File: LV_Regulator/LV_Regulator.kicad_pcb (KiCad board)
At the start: 4 copper layers, 150 x 100 mm, 199 parts, among them IC1 UCC12040DVE, IC2 MIC29152WU, IC3 MIC29152WU, J1 430450400, J2 430450400, J3 430450800, J4 430450800, J5 SWD, J6 2169890001, K1 41.52.9.005.0010, Q1 BC807, U1 ADM2483xRW, U2 STM32F103C8Tx, U3 25CSM04xxSN, U4 BQ25858QWRRVRQ1, U5 CSD19506KTT, U6 CSD19506KTT, U7 CSD19506KTT, U8 CSD19506KTT, Y1 32.768kHz, Y2 8MHz

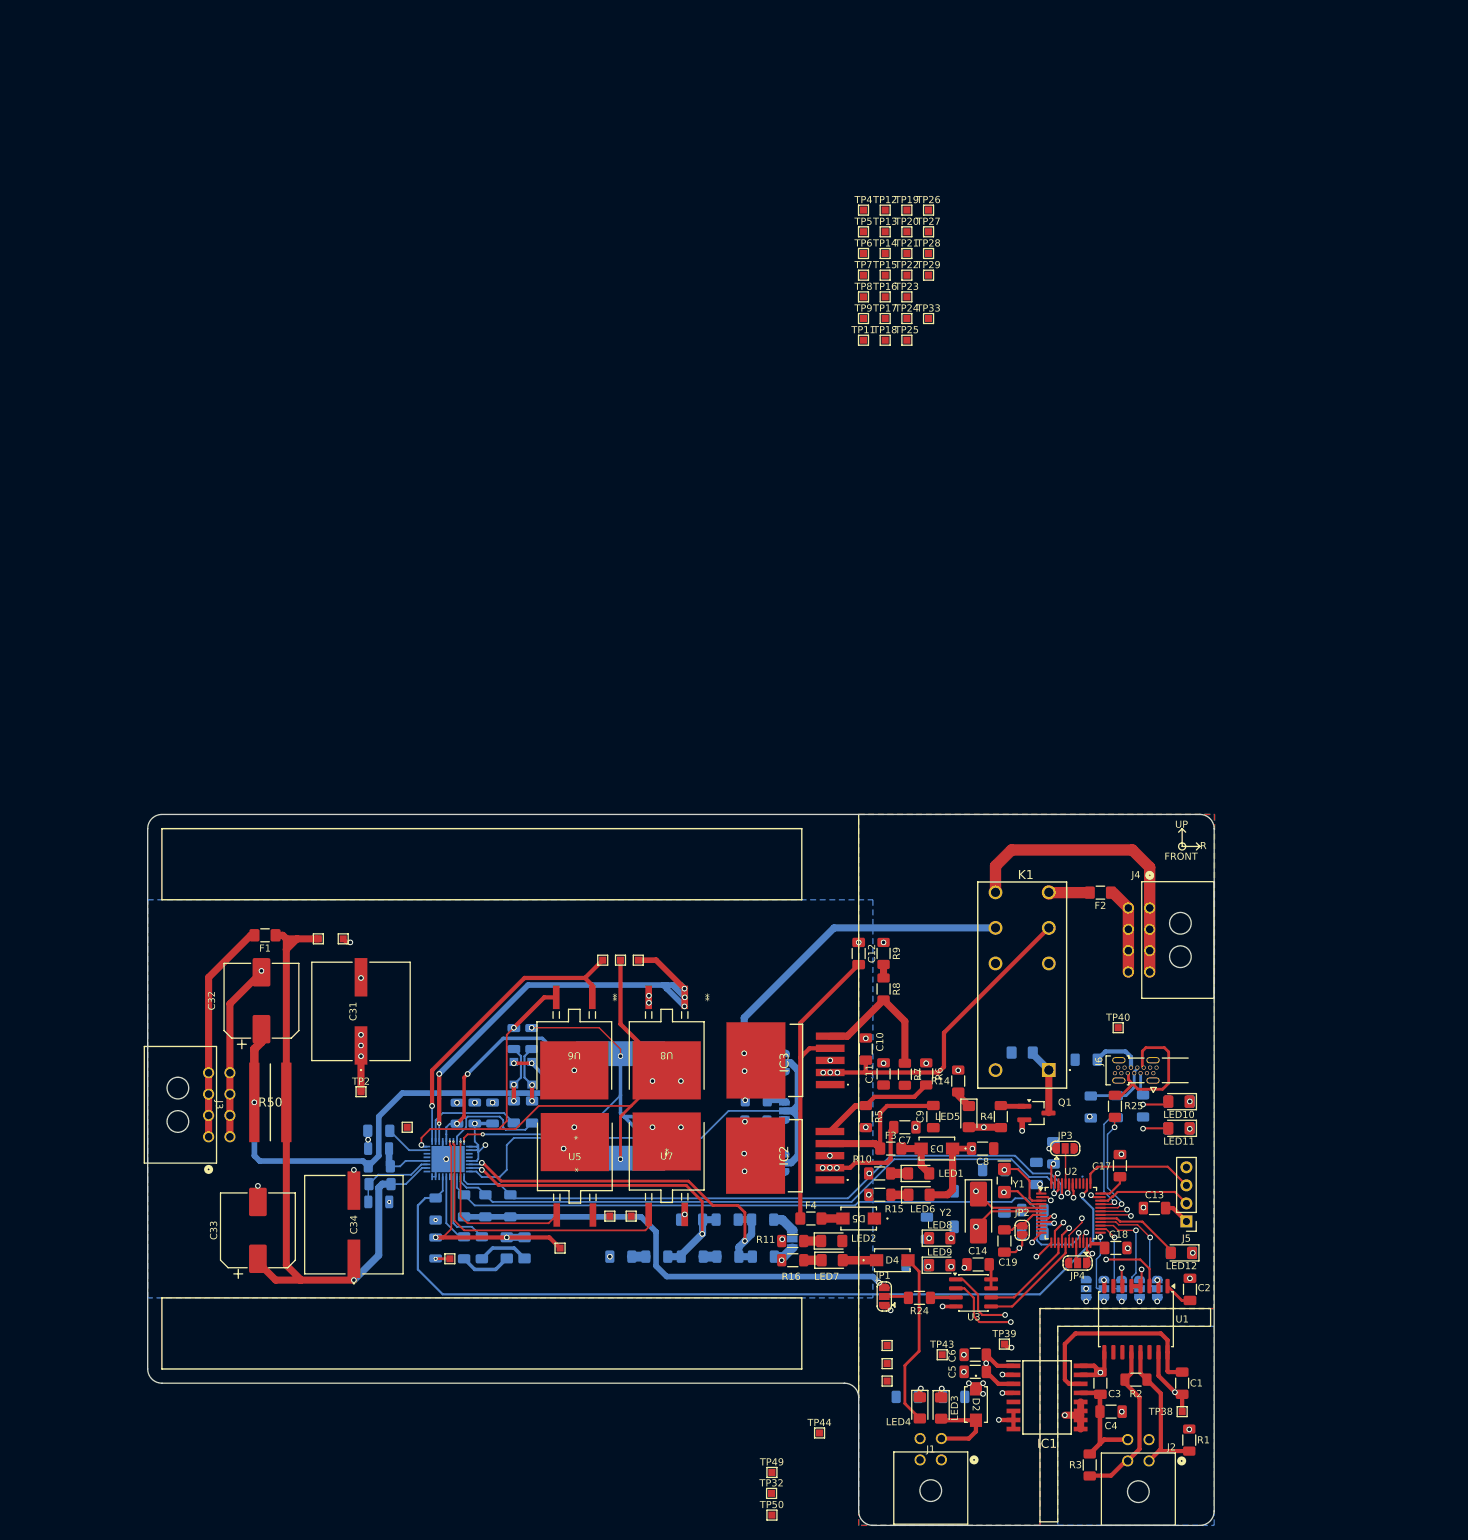
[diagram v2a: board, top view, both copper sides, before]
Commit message: Deleted Draft Regulator and Test Points Routing
Deleted Draft Routing of the Regulator and Power Electronics side of the board, because layout was not optimal in the slightest, & will replace and re-route the whole power electronics side.
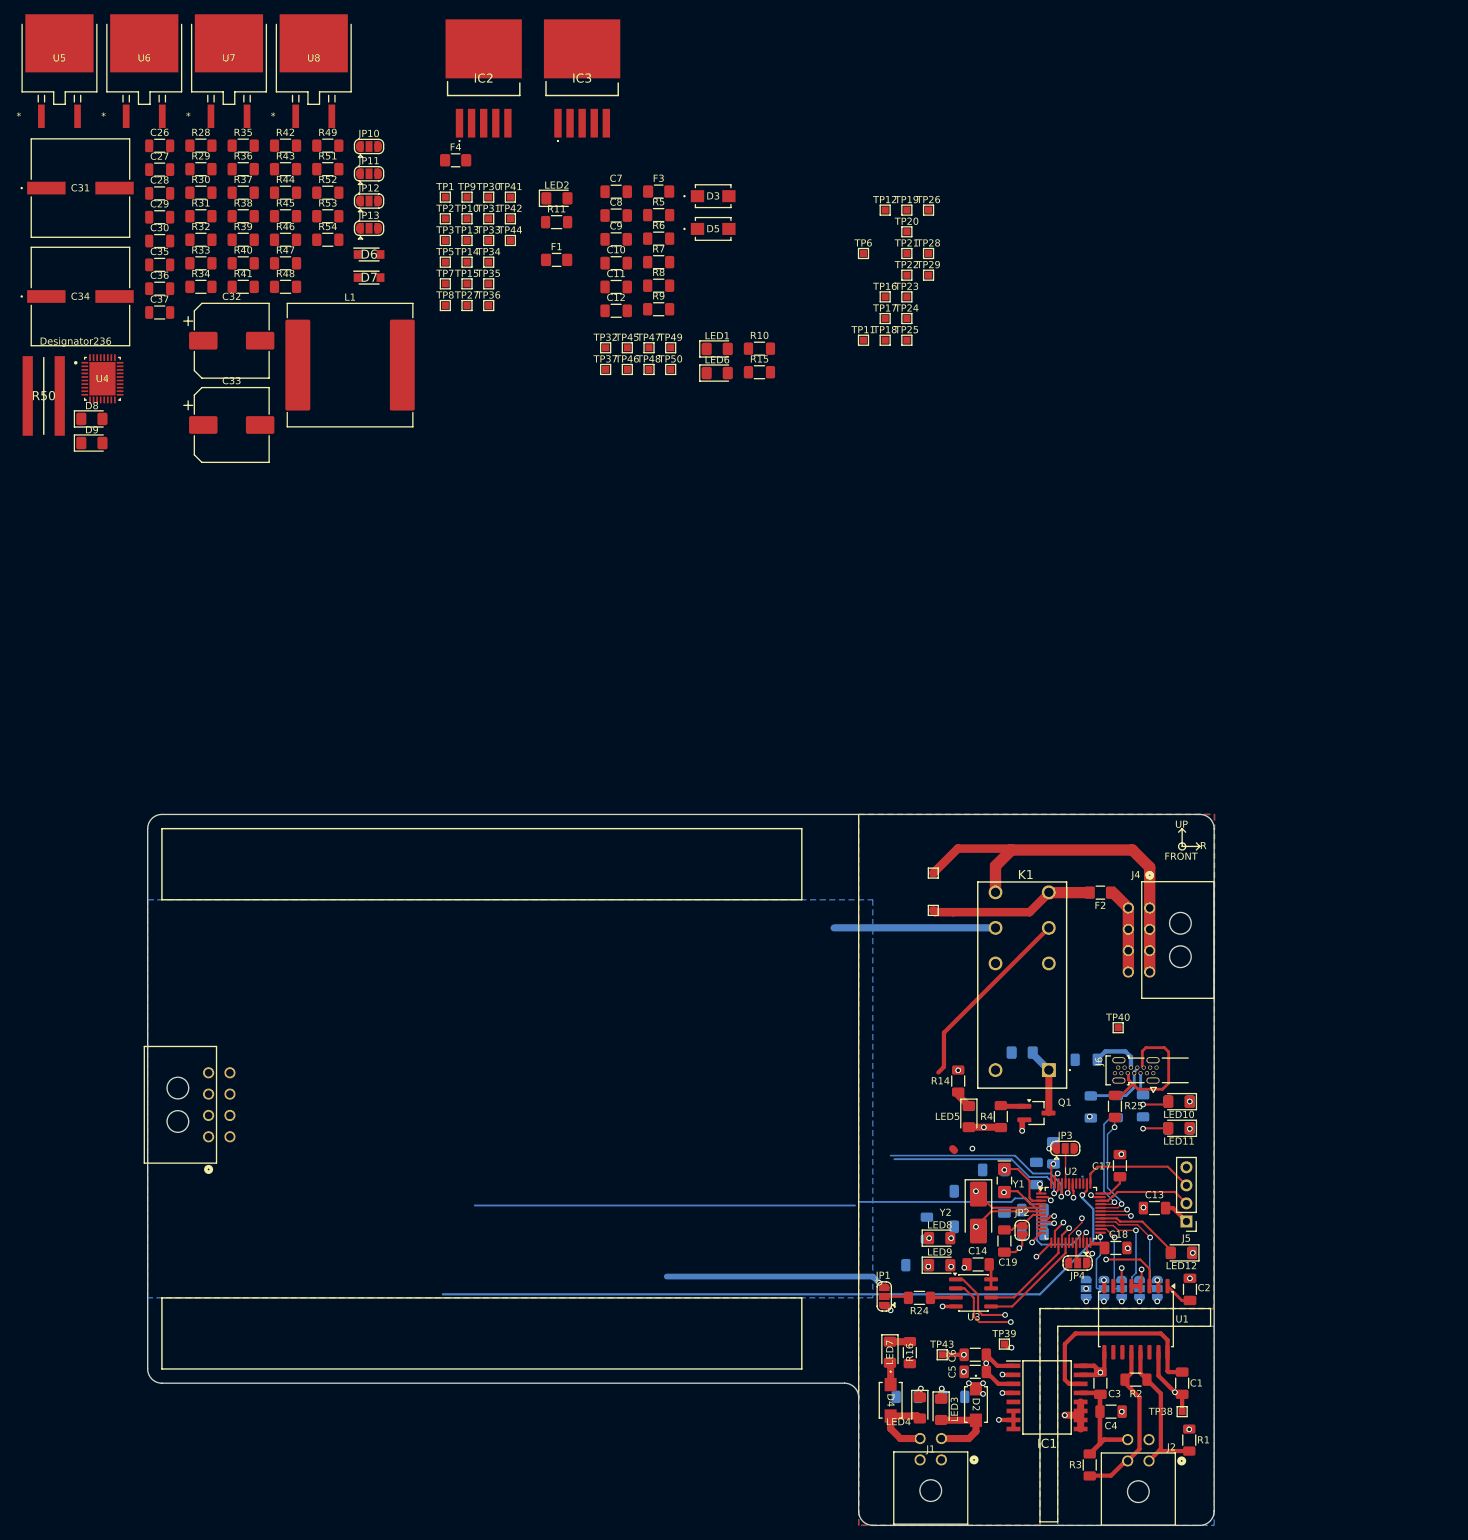
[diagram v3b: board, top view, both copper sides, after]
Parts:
- added TP45: TestPoint, TestPoint:TestPoint_Pad_1.0x1.0mm, F.Cu at (148.5, -21.6)
- added TP48: TestPoint, TestPoint:TestPoint_Pad_1.0x1.0mm, F.Cu at (151.5, -18.6)
- added TP51: 12V BAT-, TestPoint:TestPoint_Pad_1.0x1.0mm, F.Cu at (191.5, 52.2)
- C26, C27, C28, C29, C30, C35, C36, C37, D6, D7, D8, D9, JP10, JP11, JP12, JP13, L1, R28, R29, R30, R31, R32, R33, R34, R35, R36, R37, R38, R39, R40, R41, R42, R43, R44, R45, R46, R47, R48, R49, R51, R52, R53, R54, U4: moved to F.Cu
- moved TP44 173.3 mm to (132.0, -36.7)
- moved U5 170.7 mm to (68.6, -62.4)
- moved R35 166.7 mm to (94.4, -50.1), turned to 0 degrees
- moved U7 166.3 mm to (92.4, -62.4)
- moved R32 163.5 mm to (88.5, -36.8), turned to 0 degrees
- moved TP32 162.8 mm to (145.4, -21.6)
- moved R36 161.9 mm to (94.4, -46.8), turned to 0 degrees
- moved TP50 161.8 mm to (154.6, -18.6)
- moved TP49 158.8 mm to (154.6, -21.6)
- moved R33 158.2 mm to (88.5, -33.5), turned to 0 degrees
- moved R28 157.9 mm to (88.5, -50.1), turned to 0 degrees
- moved IC2 157.5 mm to (128.3, -59.7), turned to 0 degrees
- moved F4 157.0 mm to (124.3, -48.0)
- moved R30 156.0 mm to (88.5, -43.5), turned to 0 degrees
- moved R39 156.0 mm to (94.4, -36.8), turned to 0 degrees
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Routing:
- net VOUT: track 94.6 -> 0.00 mm, vias 1 -> 0
- net SW2: track 89.3 -> 0.00 mm, vias 5 -> 0
- net Net-(U6-D): track 73.5 -> 0.00 mm, vias 2 -> 0
- net Izbor_frekvencije: track 69.2 -> 0.00 mm
- net I2C_SDA: track 92.9 -> 27.0 mm
- net LODRV2_FET3: track 64.7 -> 0.00 mm, vias 5 -> 0
- net I2C_SCL: track 93.4 -> 29.3 mm
- net SW1: track 61.7 -> 0.00 mm, vias 6 -> 0
- net GND: track 111.0 -> 51.7 mm, vias 57 -> 22
- net ACUV: track 55.5 -> 0.00 mm, vias 2 -> 0
- net SYS: track 77.7 -> 26.8 mm, vias 13 -> 0
- net ACOV: track 49.6 -> 0.00 mm, vias 2 -> 0
- net Net-(IC3-OUT): track 43.9 -> 0.00 mm
- net HIDRV2_FET4: track 43.6 -> 0.00 mm, vias 1 -> 0
- net LODRV1_FET2: track 41.1 -> 0.00 mm, vias 1 -> 0
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
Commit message: Multiple Fixes in Schematic & Routing
Fixed multiple issues in schematic, like adding jumpers to isolate ACUV/ACOV between the choices. Moved the fuses on the Logic_Supply as per instruction of professor from Chair of Electronics, FoTS, UoNS. Started and made good progress on Power Electronics (Regulator Side) of the PCB.
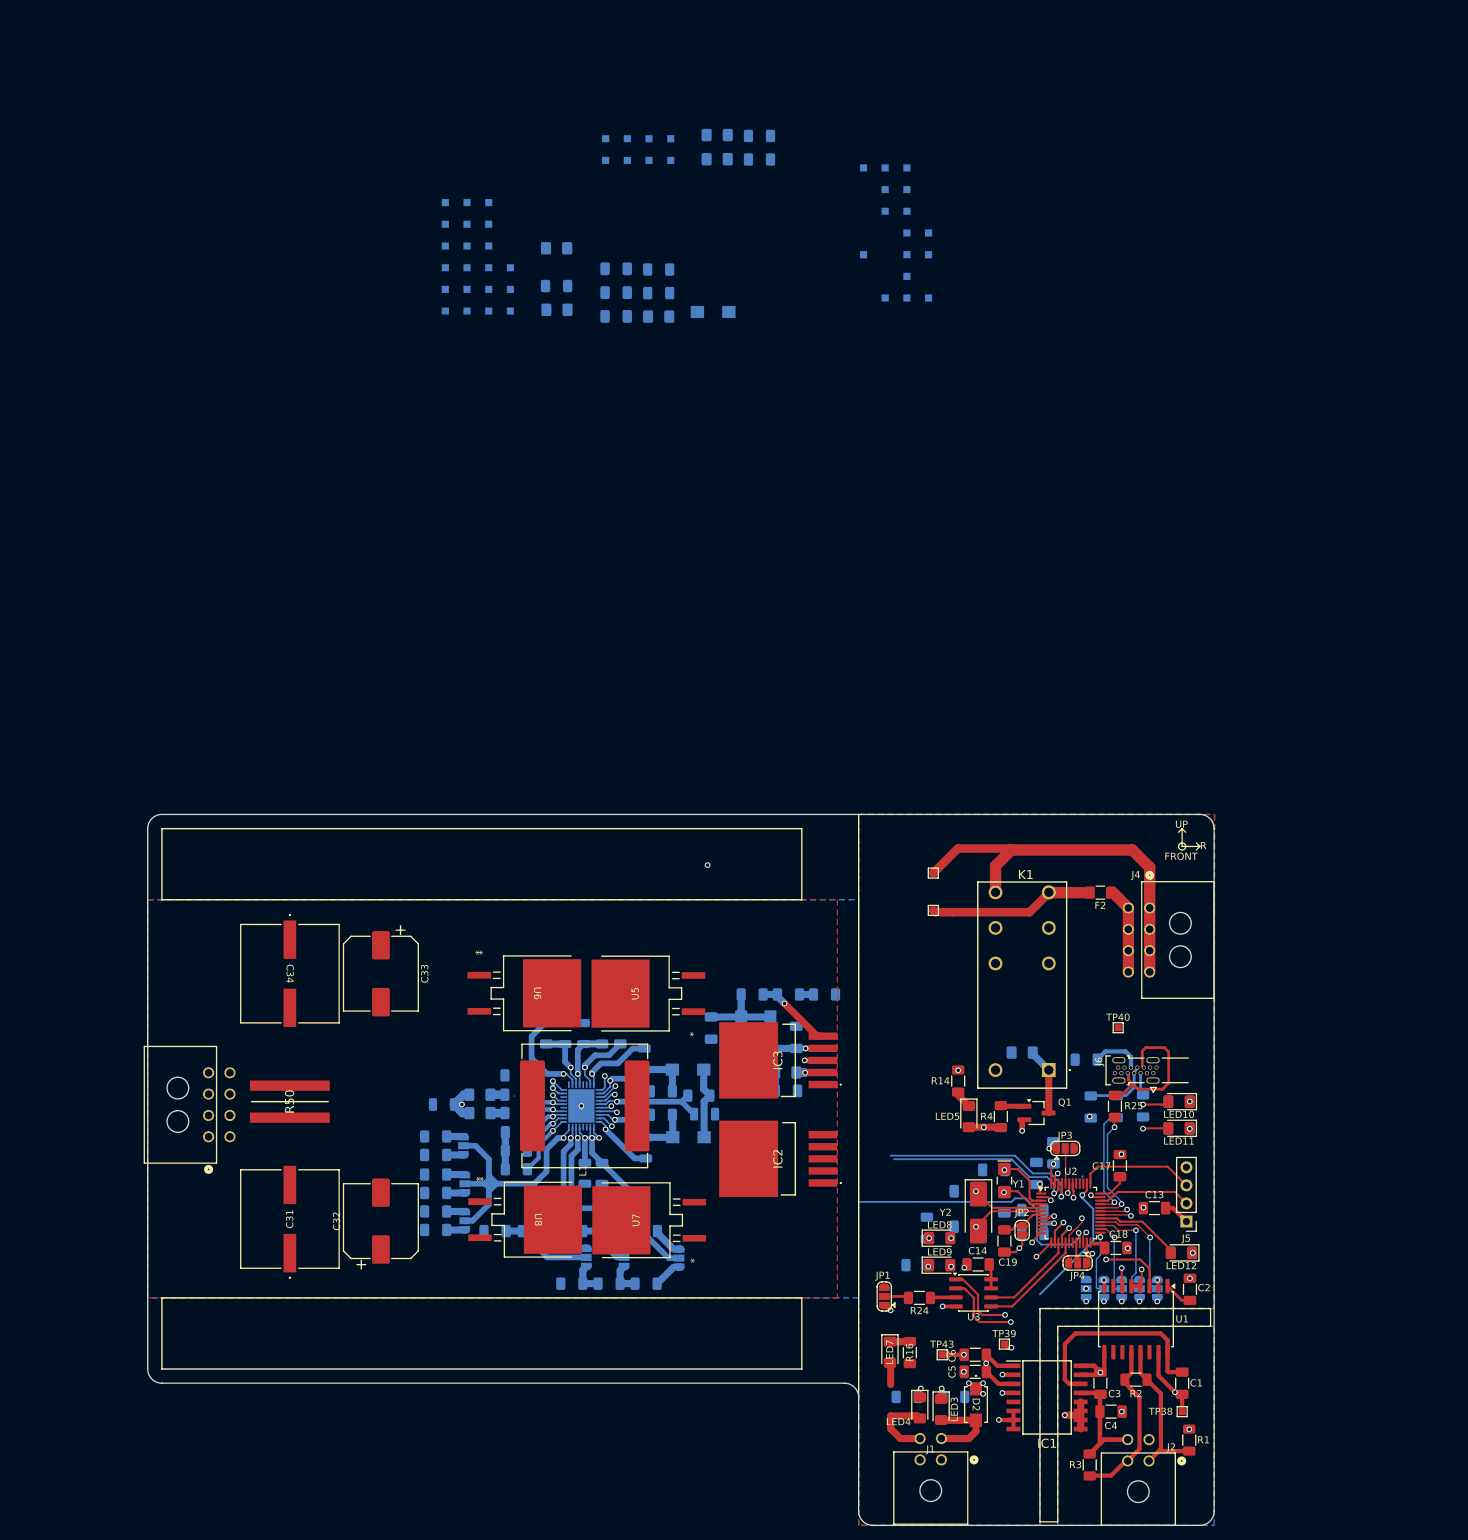
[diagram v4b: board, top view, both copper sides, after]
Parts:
- added JP14: SolderJumper_3_Open, Jumper:SolderJumper-3_P1.3mm_Open_RoundedPad1.0x1.5mm, B.Cu at (148.0, 106.3)
- added JP15: SolderJumper_3_Open, Jumper:SolderJumper-3_P1.3mm_Open_RoundedPad1.0x1.5mm, B.Cu at (142.7, 106.3)
- C10, C11, C12, C26, C27, C28, C29, C30, C35, C36, C37, C7, C8, C9, D3, D4, D5, D8, D9, F1, F3, F4, JP10, JP11, JP12, JP13, LED1, LED2, LED6, R10, R11, R15, R28, R29, R30, R31, R32, R33, R34, R35, R36, R37, R38, R39, R40, R41, R42, R43, R44, R45, R46, R47, R48, R49, R5, R51, R52, R53, R54, R6, R7, R8, R9, TP1, TP10, TP11, TP12, TP13, TP14, TP15, TP16, TP17, TP18, TP19, TP2, TP20, TP21, TP22, TP23, TP24, TP25, TP26, TP27, TP28, TP29, TP3, TP30, TP31, TP32, TP33, TP34, TP35, TP36, TP37, TP41, TP42, TP44, TP45, TP46, TP47, TP48, TP49, TP5, TP50, TP6, TP7, TP8, TP9, U4: moved to B.Cu
- D6, D7: value D_Schottky -> SS14; footprint V1FM10-M3/H:SODFL3718X108N -> SS14:CR_SMA_403AE_OSI; moved to B.Cu
- moved U7 173.2 mm to (149.7, 101.1), turned to 90 degrees
- moved U8 166.4 mm to (135.9, 101.0), turned to -90 degrees
- moved R35 158.0 mm to (135.2, 102.6), turned to 180 degrees
- moved IC2 157.6 mm to (169.5, 92.4), turned to 90 degrees
- moved R39 157.4 mm to (151.1, 110.0), turned to 180 degrees
- moved C26 156.7 mm to (151.1, 90.9), turned to 90 degrees
- moved U5 154.5 mm to (149.6, 69.2), turned to 90 degrees
- moved R36 153.5 mm to (129.8, 102.6), turned to 180 degrees
- moved R32 152.9 mm to (151.2, 102.6), turned to 180 degrees
- moved R40 152.5 mm to (145.9, 110.0), turned to 180 degrees
- moved JP13 151.3 mm to (155.8, 106.4), turned to -90 degrees
- moved C28 150.5 mm to (159.3, 86.2)
- moved R30 149.6 mm to (121.5, 102.4), turned to 180 degrees
- moved R28 148.4 mm to (121.5, 94.6), turned to 180 degrees
- moved C29 148.2 mm to (144.9, 94.5), turned to 90 degrees
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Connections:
- C12 pad 2: Net-(IC3-OUT) -> 3V3_INT
- C9 pad 2: Net-(IC2-OUT) -> 5V_INT
- F3 pad 1: Net-(IC2-OUT) -> Net-(IC2-IN)
- F3 pad 2: 5V_INT -> SYS
- F4 pad 1: Net-(IC3-OUT) -> Net-(IC3-IN)
- F4 pad 2: 3V3_INT -> SYS
- IC2 pad 2: SYS -> Net-(IC2-IN)
- IC2 pad 4: Net-(IC2-OUT) -> 5V_INT
- IC3 pad 2: SYS -> Net-(IC3-IN)
- IC3 pad 4: Net-(IC3-OUT) -> 3V3_INT
- JP13 pad 2: VAC_OV_UV_VIN -> SYS
- R32 pad 2: ACUV -> Net-(JP14-B)
- R33 pad 1: ACUV -> Net-(JP14-B)
- R34 pad 2: ACOV -> Net-(JP15-B)
- R35 pad 1: ACOV -> Net-(JP15-B)
- R39 pad 2: ACUV -> Net-(JP14-A)
- R40 pad 1: ACUV -> Net-(JP14-A)
- R40 pad 2: ACOV -> Net-(JP15-A)
- R41 pad 1: ACOV -> Net-(JP15-A)
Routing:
- net CE_N: track 103.7 -> 21.5 mm, vias 1 -> 2
- net INT_N: track 92.4 -> 45.0 mm, vias 1 -> 2
- net Izbor_frekvencije: track 0.00 -> 40.6 mm, vias 0 -> 1
- net ACOV: track 0.00 -> 26.9 mm, vias 0 -> 1
- net ACUV: track 0.00 -> 24.3 mm, vias 0 -> 1
- net DRV_SUPPLY: track 0.00 -> 15.6 mm, vias 0 -> 1
- net VBAT: track 61.8 -> 47.4 mm, vias 10 -> 9
- net VOUT: track 0.00 -> 13.7 mm, vias 0 -> 1
- net Net-(IC3-ADJ): track 0.00 -> 11.0 mm, vias 0 -> 1
- net SW2: track 0.00 -> 10.6 mm, vias 0 -> 1
- net Net-(D6-A): track 0.00 -> 10.2 mm
- net GND: track 51.7 -> 41.6 mm, vias 22 -> 27
- net SYS: track 26.8 -> 36.2 mm, vias 0 -> 3
- net BTST2: track 0.00 -> 9.31 mm, vias 0 -> 1
- net Net-(U4-MODE): track 0.00 -> 9.26 mm, vias 0 -> 1
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- added copper zone on In2.Cu, net GND
- added copper zone on F.Cu, net SYS
- added copper zone on In1.Cu, net VOUT
- removed copper zone on In2.Cu, net SYS
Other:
- board text added: "When selecting ACOV/ACUV input protection value, short ONLY one side either Left or Right. Input choices are: 19-48V - R39,R40,R41 12V - R32,R33,R34,R35,R36 For anything else look in manual"
- board text added: "When selecting FSW value short ONLY 1 pad for 1 R Selectable frequencies: Rfsw1: 132k - R28 - 250kHZ Rfsw2: 100k - R30 - 300kHZ Rfsw3: 80k - R37 - 350kHZ Rfsw4: 67k - R29 - 400kHZ Rfsw5: 57k - R31 - 450kHZ Rfsw6: 50k - R38 - 500kHZ"
